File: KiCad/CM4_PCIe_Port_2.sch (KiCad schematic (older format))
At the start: 3 parts, among them J13 PCIe_x16

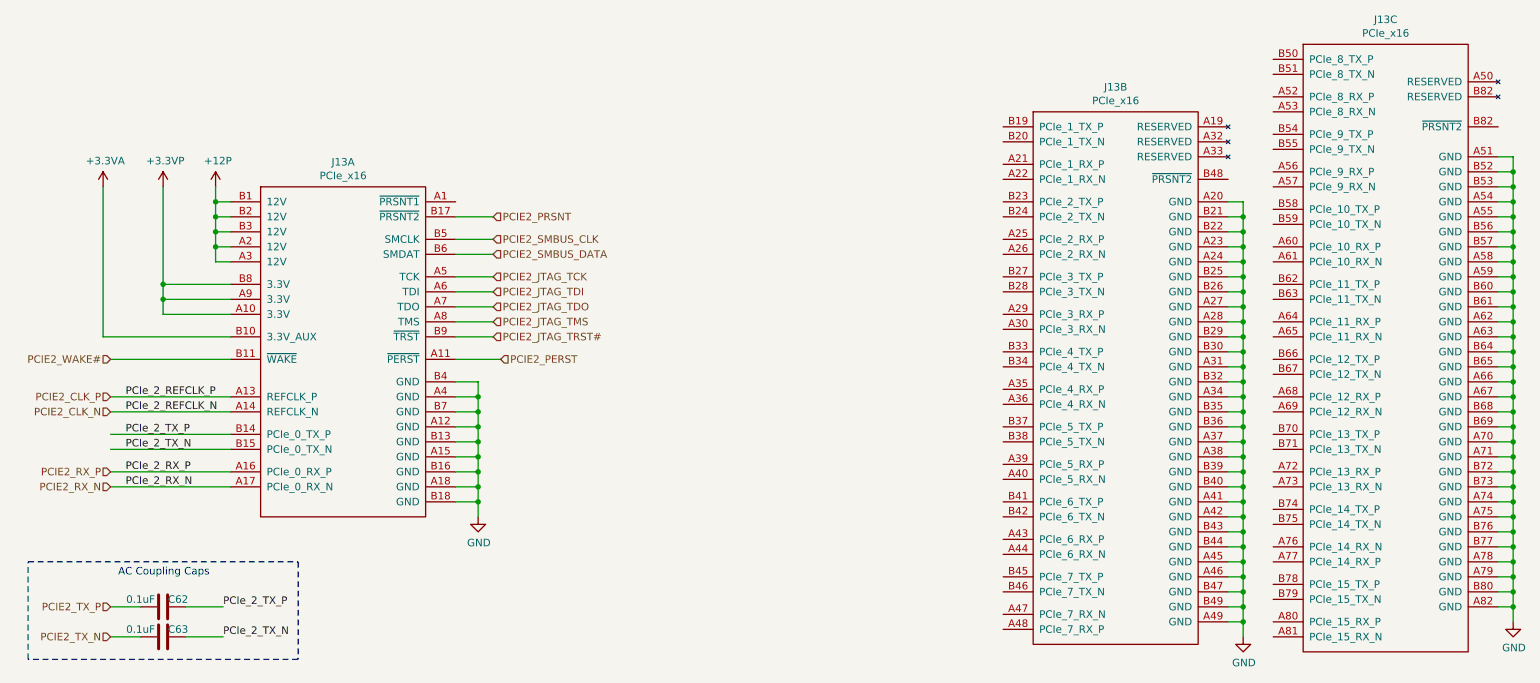
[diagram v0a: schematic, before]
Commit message: Tons of wiring and pin straps for PCI-e Switch
Also re-did some hierarchical labels for JTAG
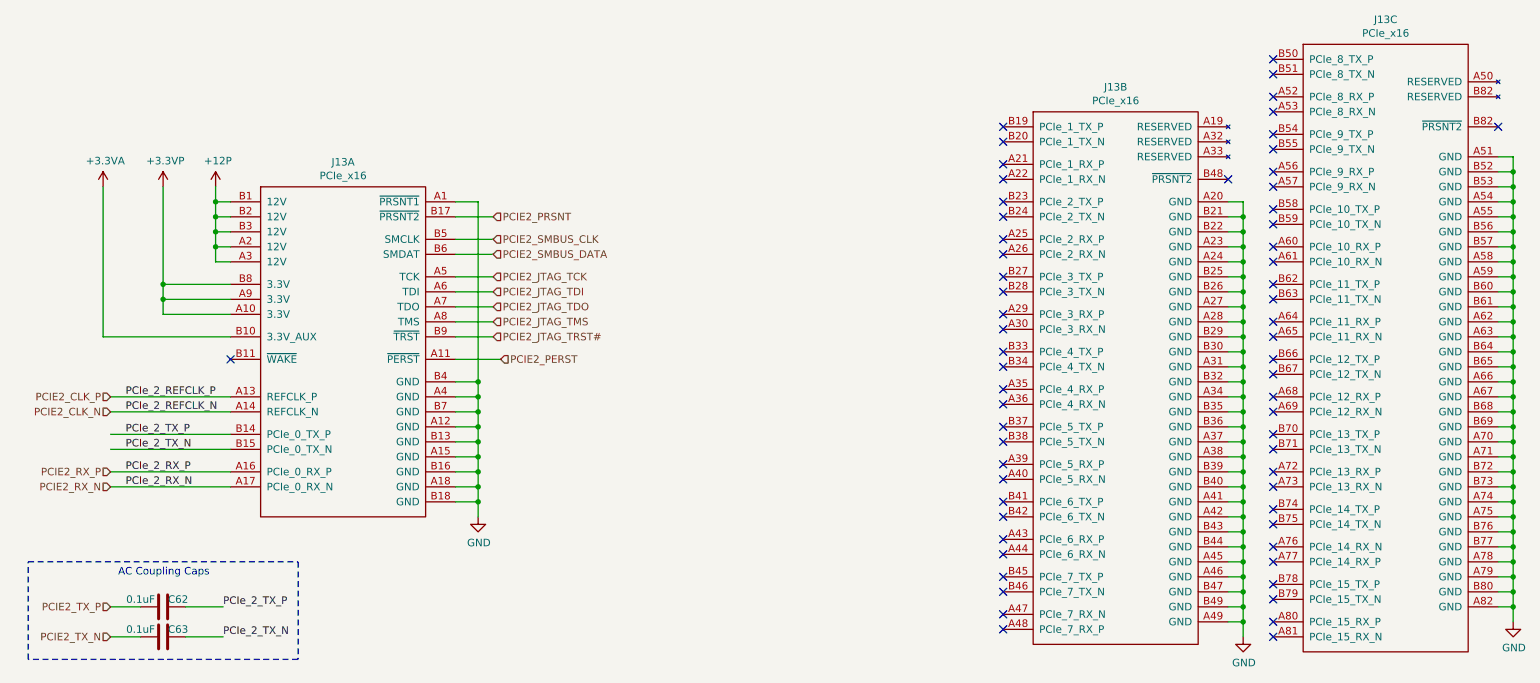
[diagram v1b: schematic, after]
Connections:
- net GND: now also J13.A1 (~PRSNT1)
- net PCIE2_WAKE#: no longer names the net of J13.B11 (~WAKE)
- no-connect marks 0 -> 63
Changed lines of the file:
@@
 PCIE2_SMBUS_DATA
-Wire Wire Line
-	2250 3700 1450 3700
-Text HLabel 1450 3700 0    50   Input ~ 0
-PCIE2_WAKE#
 Wire Wire Line
 	3750 3150 4000 3150
@@
 Text HLabel 4000 3550 2    50   Input ~ 0
 PCIE2_JTAG_TRST#
+NoConn ~ 7400 2150
+NoConn ~ 7400 2250
+NoConn ~ 7400 2400
+NoConn ~ 7400 2500
+NoConn ~ 7400 2650
+NoConn ~ 7400 2750
+NoConn ~ 8900 2500
+NoConn ~ 9200 1700
+NoConn ~ 9200 1800
+NoConn ~ 9200 1950
+NoConn ~ 9200 2050
+NoConn ~ 9200 2200
+NoConn ~ 9200 2300
+NoConn ~ 9200 2450
+NoConn ~ 9200 2550
+NoConn ~ 9200 2700
+NoConn ~ 9200 2800
+NoConn ~ 9200 2950
+NoConn ~ 9200 3050
+NoConn ~ 9200 3200
+NoConn ~ 9200 3300
+NoConn ~ 9200 3450
+NoConn ~ 9200 3550
+NoConn ~ 9200 3700
+NoConn ~ 9200 3800
+NoConn ~ 9200 3950
+NoConn ~ 9200 4050
+NoConn ~ 7400 4000
+NoConn ~ 7400 3900
+NoConn ~ 7400 3750
+NoConn ~ 7400 3650
+NoConn ~ 7400 3500
+NoConn ~ 7400 3400
+NoConn ~ 7400 3250
+NoConn ~ 7400 3150
+NoConn ~ 7400 3000
+NoConn ~ 7400 2900
+NoConn ~ 7400 4150
+NoConn ~ 7400 4250
+NoConn ~ 7400 4400
+NoConn ~ 7400 4500
+NoConn ~ 7400 4650
+NoConn ~ 7400 4750
+NoConn ~ 7400 4900
+NoConn ~ 7400 5000
+NoConn ~ 7400 5150
+NoConn ~ 7400 5250
+NoConn ~ 7400 5400
+NoConn ~ 7400 5500
+NoConn ~ 9200 5550
+NoConn ~ 9200 5450
+NoConn ~ 9200 5300
+NoConn ~ 9200 5200
+NoConn ~ 9200 5050
+NoConn ~ 9200 4950
+NoConn ~ 9200 4800
+NoConn ~ 9200 4700
+NoConn ~ 9200 4550
+NoConn ~ 9200 4450
+NoConn ~ 9200 4300
+NoConn ~ 9200 4200
+NoConn ~ 10700 2150
+Wire Wire Line
+	3750 2650 3900 2650
+Wire Wire Line
+	3900 2650 3900 3850
+Connection ~ 3900 3850
+NoConn ~ 2250 3700
 $EndSCHEMATC

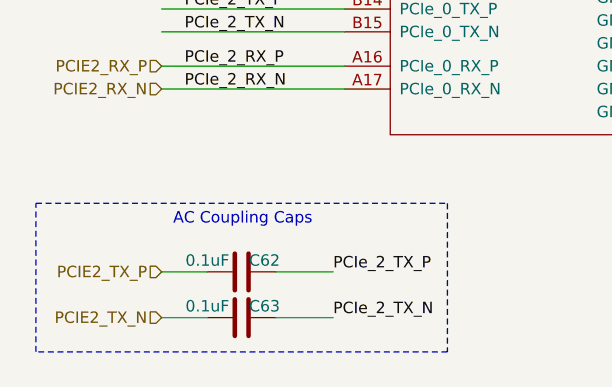
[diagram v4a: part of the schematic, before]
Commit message: Started picking passive components, overhauled library
Cleaned up a bunch of schematic library references.
Added datasheets, descriptions for a lot of existing parts.
Picked most capacitor parts, still a couple left.
Cleaned up a fair few footprint references.
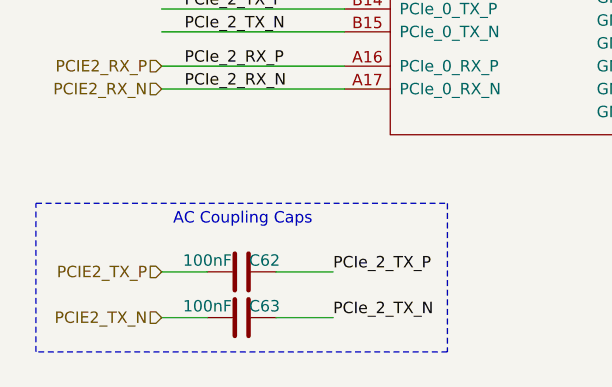
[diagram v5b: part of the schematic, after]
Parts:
- C62, C63: value 0.1uF -> 100nF; footprint (none) -> CM4_MATX:C_0402_1005Metric_Pad0.74x0.62mm_HandSolder; Description (none) -> 10V 0.1uF X5R 0402 20% Tol; Mfr. (none) -> AVX; Mfr. No (none) -> 0402ZD104MAT4A; Mouser Part Number (none) -> 581-0402ZD104MAT4A; Mouser Price/Stock (none) -> https://www.mouser.co.uk/ProductDetail/AVX/0402ZD104MAT4A/?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
- J13: Description (none) -> Amphenol FCI PCI-e x16 Connector 164 POS; Mfr. (none) -> Amphenol; Mfr. No (none) -> 10018783-10113TLF; Mouser Part Number (none) -> 649-18783-10113TLF; Mouser Price/Stock (none) -> https://www.mouser.co.uk/ProductDetail/Amphenol-FCI/1001878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
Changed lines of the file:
@@
 PCIE2_TX_P
 $Comp
-L power:GND #PWR?
+L CM4_MATX:GND #PWR?
 U 1 1 5FEA62ED
 P 3900 4750
@@
 PCIe_2_RX_N
 $Comp
-L power:+12P #PWR?
+L CM4_MATX:+12P #PWR?
 U 1 1 5FEA6319
 P 2150 2550
@@
 	2150 2650 2150 2550
 $Comp
-L power:+3.3VP #PWR?
+L CM4_MATX:+3.3VP #PWR?
 U 1 1 5FEA632D
 P 1800 2550
@@
 	1800 3200 1800 2550
 $Comp
-L power:+3.3VA #PWR?
+L CM4_MATX:+3.3VA #PWR?
 U 1 1 5FEA633B
 P 1400 2550
@@
 F 1 "PCIe_x16" H 3000 6324 50  0000 C CNN
 F 2 "CM4_MATX:10018783-10113TLF" H 1250 8800 50  0001 C CNN
-F 3 "" H 1250 8800 50  0001 C CNN
+F 3 "https://www.amphenol-icc.com/media/wysiwyg/files/documentation/datasheet/ssio/ssio_pcie_gen3.pdf" H 1250 8800 50  0001 C CNN
+F 4 "Amphenol FCI PCI-e x16 Connector 164 POS" H 3050 4400 50  0001 C CNN "Description"
+F 5 "649-18783-10113TLF" H 3050 4400 50  0001 C CNN "Mouser Part Number"
+F 6 "https://www.mouser.co.uk/ProductDetail/Amphenol-FCI/10018783-10113TLF/?qs=%2Fha2pyFadugRWVTwF3IyzEudyJIuC5mu1uxWW1BR%252B5VORiWMhxM3Zw%3D%3D" H 3050 4400 50  0001 C CNN "Mouser Price/Stock"
+F 7 "Amphenol" H 3050 4400 50  0001 C CNN "Mfr."
+F 8 "10018783-10113TLF" H 3050 4400 50  0001 C CNN "Mfr. No"
 	1    3050 4400
 	1    0    0    -1
@@
 F 1 "PCIe_x16" H 8150 5824 50  0000 C CNN
 F 2 "CM4_MATX:10018783-10113TLF" H 6350 8300 50  0001 C CNN
-F 3 "" H 6350 8300 50  0001 C CNN
+F 3 "https://www.amphenol-icc.com/media/wysiwyg/files/documentation/datasheet/ssio/ssio_pcie_gen3.pdf" H 6350 8300 50  0001 C CNN
+F 4 "Amphenol FCI PCI-e x16 Connector 164 POS" H 8150 3900 50  0001 C CNN "Description"
+F 5 "649-18783-10113TLF" H 8150 3900 50  0001 C CNN "Mouser Part Number"
+F 6 "https://www.mouser.co.uk/ProductDetail/Amphenol-FCI/10018783-10113TLF/?qs=%2Fha2pyFadugRWVTwF3IyzEudyJIuC5mu1uxWW1BR%252B5VORiWMhxM3Zw%3D%3D" H 8150 3900 50  0001 C CNN "Mouser Price/Stock"
+F 7 "Amphenol" H 8150 3900 50  0001 C CNN "Mfr."
+F 8 "10018783-10113TLF" H 8150 3900 50  0001 C CNN "Mfr. No"
 	2    8150 3900
 	1    0    0    -1
@@
 F 1 "PCIe_x16" H 9950 5374 50  0000 C CNN
 F 2 "CM4_MATX:10018783-10113TLF" H 8150 7850 50  0001 C CNN
-F 3 "" H 8150 7850 50  0001 C CNN
+F 3 "https://www.amphenol-icc.com/media/wysiwyg/files/documentation/datasheet/ssio/ssio_pcie_gen3.pdf" H 8150 7850 50  0001 C CNN
+F 4 "Amphenol FCI PCI-e x16 Connector 164 POS" H 9950 3450 50  0001 C CNN "Description"
+F 5 "649-18783-10113TLF" H 9950 3450 50  0001 C CNN "Mouser Part Number"
+F 6 "https://www.mouser.co.uk/ProductDetail/Amphenol-FCI/10018783-10113TLF/?qs=%2Fha2pyFadugRWVTwF3IyzEudyJIuC5mu1uxWW1BR%252B5VORiWMhxM3Zw%3D%3D" H 9950 3450 50  0001 C CNN "Mouser Price/Stock"
+F 7 "Amphenol" H 9950 3450 50  0001 C CNN "Mfr."
+F 8 "10018783-10113TLF" H 9950 3450 50  0001 C CNN "Mfr. No"
 	3    9950 3450
 	1    0    0    -1
@@
 	10800 5350 10800 5450
 $Comp
-L power:GND #PWR0189
+L CM4_MATX:GND #PWR0189
 U 1 1 600B9F64
 P 10800 5450
@@
 $EndComp
 $Comp
-L power:GND #PWR0190
+L CM4_MATX:GND #PWR0190
 U 1 1 600BA254
 P 9000 5550
@@
 AR Path="/5FFBC089/5FFBFF20/5FF242AA" Ref="C63"  Part="1"
 F 0 "C63" V 1750 5650 50  0000 C CNN
-F 1 "0.1uF" V 1750 5400 50  0000 C CNN
-F 2 "" H 1838 5400 50  0001 C CNN
-F 3 "~" H 1800 5550 50  0001 C CNN
+F 1 "100nF" V 1750 5400 50  0000 C CNN
+F 2 "CM4_MATX:C_0402_1005Metric_Pad0.74x0.62mm_HandSolder" H 1838 5400 50  0001 C CNN
+F 3 "https://www.mouser.co.uk/datasheet/2/40/cx5r-776519.pdf" H 1800 5550 50  0001 C CNN
+F 4 "581-0402ZD104MAT4A" H 1800 5550 50  0001 C CNN "Mouser Part Number"
+F 5 "https://www.mouser.co.uk/ProductDetail/AVX/0402ZD104MAT4A/?qs=sGAEpiMZZMvsSlwiRhF8qud6rLLpfNdE%2FYSoyEGdkn4%3D" H 1800 5550 50  0001 C CNN "Mouser Price/Stock"
+F 6 "AVX" H 1800 5550 50  0001 C CNN "Mfr."
+F 7 "0402ZD104MAT4A" H 1800 5550 50  0001 C CNN "Mfr. No"
+F 8 "10V 0.1uF X5R 0402 20% Tol" H 1800 5550 50  0001 C CNN "Description"
 	1    1800 5550
 	0    1    1    0
@@
 AR Path="/5FFBC089/5FFBFF20/5FF242B0" Ref="C62"  Part="1"
 F 0 "C62" V 1850 5250 50  0000 C CNN
-F 1 "0.1uF" V 1850 5500 50  0000 C CNN
-F 2 "" H 1838 5200 50  0001 C CNN
-F 3 "~" H 1800 5350 50  0001 C CNN
+F 1 "100nF" V 1850 5500 50  0000 C CNN
+F 2 "CM4_MATX:C_0402_1005Metric_Pad0.74x0.62mm_HandSolder" H 1838 5200 50  0001 C CNN
+F 3 "https://www.mouser.co.uk/datasheet/2/40/cx5r-776519.pdf" H 1800 5350 50  0001 C CNN
+F 4 "581-0402ZD104MAT4A" H 1800 5350 50  0001 C CNN "Mouser Part Number"
+F 5 "https://www.mouser.co.uk/ProductDetail/AVX/0402ZD104MAT4A/?qs=sGAEpiMZZMvsSlwiRhF8qud6rLLpfNdE%2FYSoyEGdkn4%3D" H 1800 5350 50  0001 C CNN "Mouser Price/Stock"
+F 6 "AVX" H 1800 5350 50  0001 C CNN "Mfr."
+F 7 "0402ZD104MAT4A" H 1800 5350 50  0001 C CNN "Mfr. No"
+F 8 "10V 0.1uF X5R 0402 20% Tol" H 1800 5350 50  0001 C CNN "Description"
 	1    1800 5350
 	0    -1   -1   0

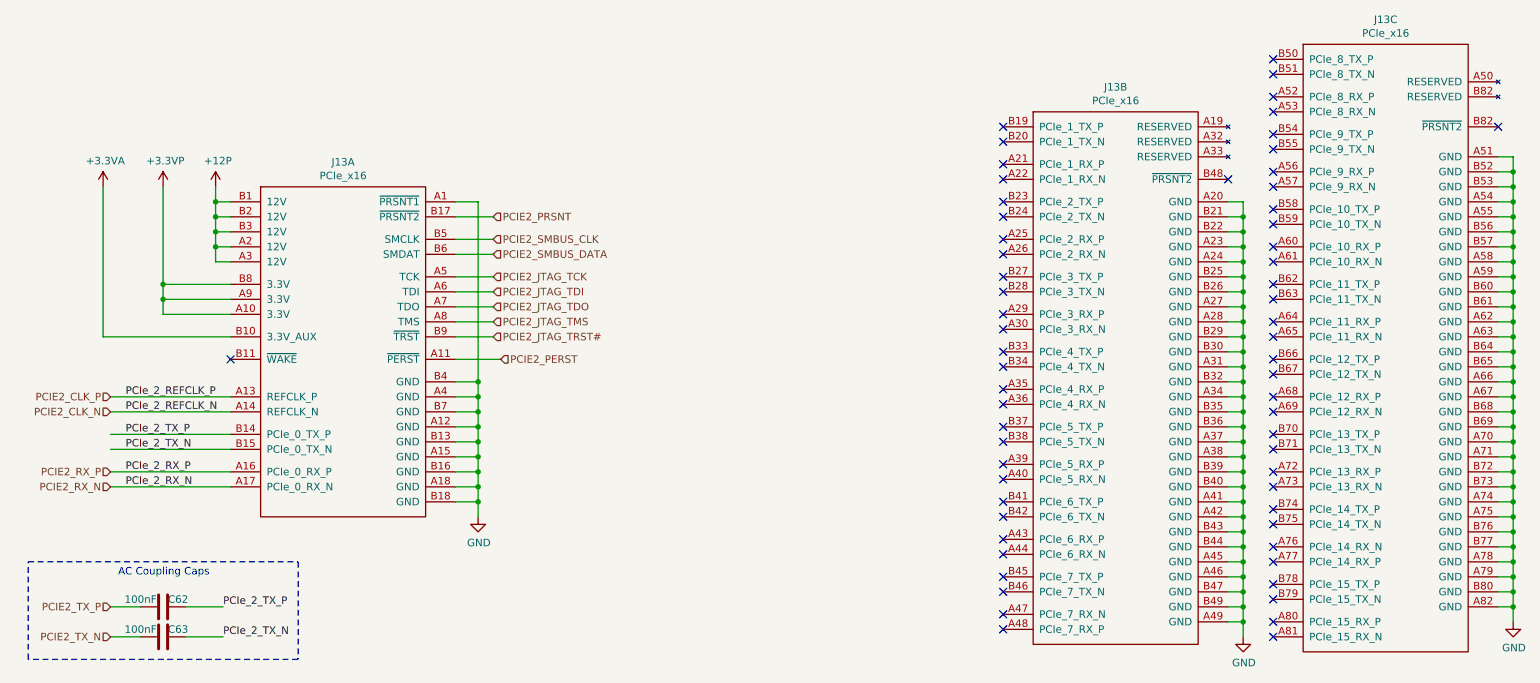
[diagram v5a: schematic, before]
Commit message: Imported new components to the PCB and moved some components
Updated PDFs and added two new board layers. One for ground and a second for power (voltage to be decided)
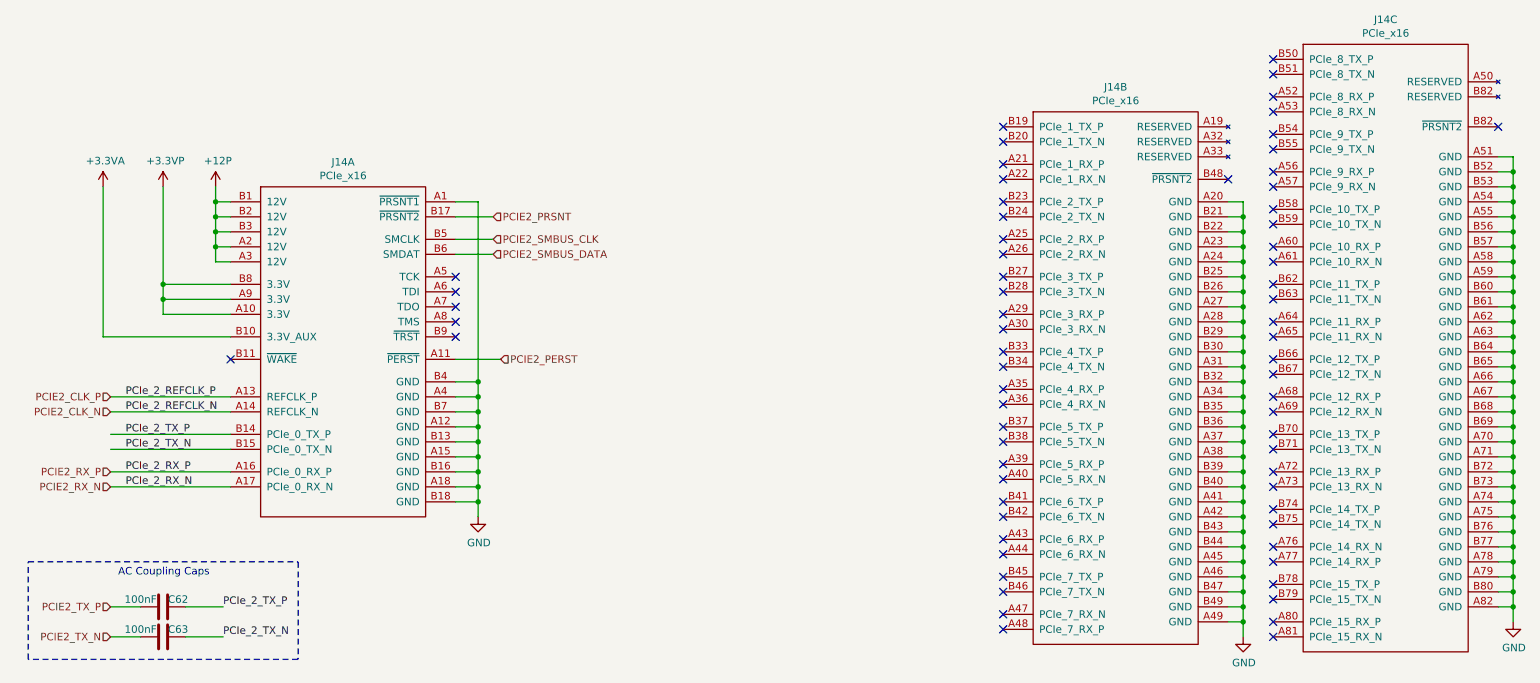
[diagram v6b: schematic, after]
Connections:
- net PCIE2_JTAG_TCK: no longer names the net of J13.A5 (TCK)
- net PCIE2_JTAG_TDI: no longer names the net of J13.A6 (TDI)
- net PCIE2_JTAG_TDO: no longer names the net of J13.A7 (TDO)
- net PCIE2_JTAG_TMS: no longer names the net of J13.A8 (TMS)
- net PCIE2_JTAG_TRST#: no longer names the net of J13.B9 (~TRST)
- no-connect marks 63 -> 68
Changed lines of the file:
@@
 $Descr A4 11693 8268
 encoding utf-8
-Sheet 16 16
+Sheet 15 15
 Title "PCIe x16 - Slot 2"
 Date "2021-02-08"
@@
 P 3050 4400
 AR Path="/5FD73012/5FED8C9C" Ref="J13"  Part="1"
-AR Path="/5FFBC089/5FFBFF20/5FED8C9C" Ref="J13"  Part="1"
-F 0 "J13" H 3000 6415 50  0000 C CNN
+AR Path="/5FFBC089/5FFBFF20/5FED8C9C" Ref="J14"  Part="1"
+F 0 "J14" H 3000 6415 50  0000 C CNN
 F 1 "PCIe_x16" H 3000 6324 50  0000 C CNN
 F 2 "CM4_MATX:10018783-10113TLF" H 1250 8800 50  0001 C CNN
@@
 P 8150 3900
 AR Path="/5FD73012/5FEDF22E" Ref="J13"  Part="2"
-AR Path="/5FFBC089/5FFBFF20/5FEDF22E" Ref="J13"  Part="2"
-F 0 "J13" H 8150 5915 50  0000 C CNN
+AR Path="/5FFBC089/5FFBFF20/5FEDF22E" Ref="J14"  Part="2"
+F 0 "J14" H 8150 5915 50  0000 C CNN
 F 1 "PCIe_x16" H 8150 5824 50  0000 C CNN
 F 2 "CM4_MATX:10018783-10113TLF" H 6350 8300 50  0001 C CNN
@@
 P 9950 3450
 AR Path="/5FD73012/5FEE2CC4" Ref="J13"  Part="3"
-AR Path="/5FFBC089/5FFBFF20/5FEE2CC4" Ref="J13"  Part="3"
-F 0 "J13" H 9950 5465 50  0000 C CNN
+AR Path="/5FFBC089/5FFBFF20/5FEE2CC4" Ref="J14"  Part="3"
+F 0 "J14" H 9950 5465 50  0000 C CNN
 F 1 "PCIe_x16" H 9950 5374 50  0000 C CNN
 F 2 "CM4_MATX:10018783-10113TLF" H 8150 7850 50  0001 C CNN
@@
 Text HLabel 4000 3000 2    50   Input ~ 0
 PCIE2_SMBUS_DATA
-Wire Wire Line
-	3750 3150 4000 3150
-Wire Wire Line
-	3750 3250 4000 3250
-Wire Wire Line
-	3750 3350 4000 3350
-Wire Wire Line
-	3750 3450 4000 3450
-Wire Wire Line
-	3750 3550 4000 3550
-Text HLabel 4000 3150 2    50   Input ~ 0
-PCIE2_JTAG_TCK
-Text HLabel 4000 3250 2    50   Input ~ 0
-PCIE2_JTAG_TDI
-Text HLabel 4000 3350 2    50   Input ~ 0
-PCIE2_JTAG_TDO
-Text HLabel 4000 3450 2    50   Input ~ 0
-PCIE2_JTAG_TMS
-Text HLabel 4000 3550 2    50   Input ~ 0
-PCIE2_JTAG_TRST#
 NoConn ~ 7400 2150
 NoConn ~ 7400 2250
@@
 Connection ~ 3900 3850
 NoConn ~ 2250 3700
+NoConn ~ 3750 3550
+NoConn ~ 3750 3450
+NoConn ~ 3750 3350
+NoConn ~ 3750 3250
+NoConn ~ 3750 3150
 $EndSCHEMATC
